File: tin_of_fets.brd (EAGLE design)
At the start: 28.6 x 55.9 mm, 49 parts, among them Q1 J112, Q2 J112, Q3 ZVN4306A, Q4 ZVN4306A, Q5 J112, Q6 J112, Q7 ZVN4306A, Q8 ZVN4306A, T1 ZTX694B

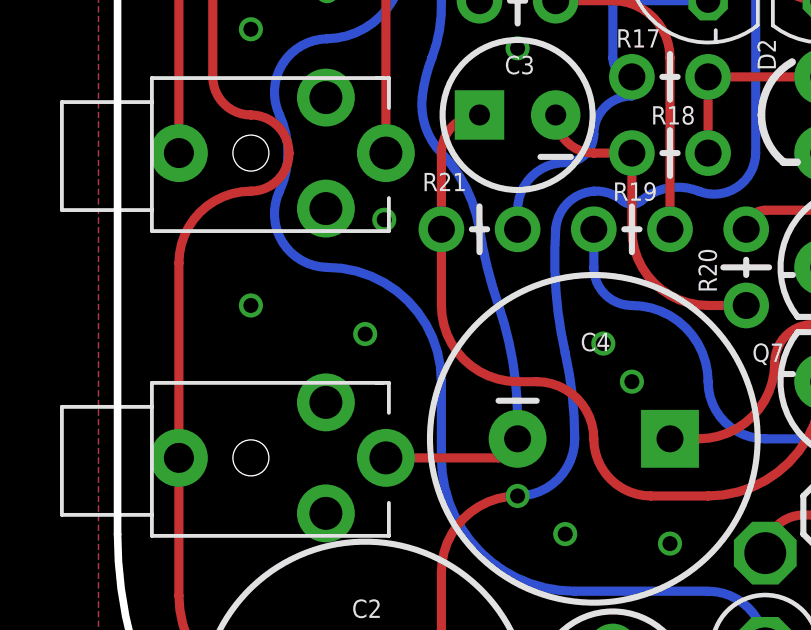
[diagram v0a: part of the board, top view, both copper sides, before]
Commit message: Single bypass cap. No more room
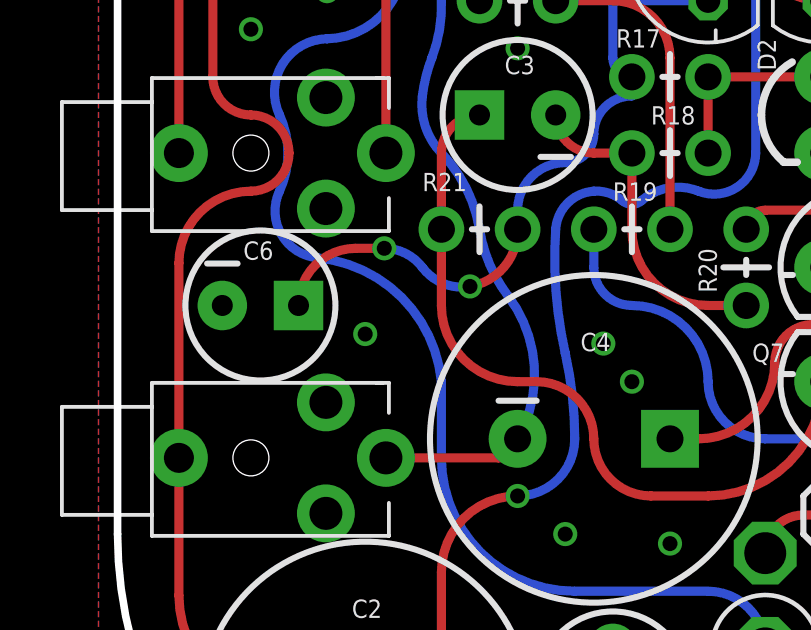
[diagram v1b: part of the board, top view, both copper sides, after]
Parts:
- added C6: 10uF, SparkFun-Capacitors:CPOL-RADIAL-10UF-25V
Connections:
- net GND: now also C6.2
- net VCC: now also C6.1
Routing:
- net VCC: track 39.2 -> 48.5 mm, vias 0 -> 2
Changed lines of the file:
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@@
 </element>
 <element name="J4" library="SparkFun-Connectors" package="STEREOJACK2.5MM_STEREOJACK2.5MM" value="" x="25.4" y="3.81" smashed="yes" rot="R90"/>
+<element name="C6" library="SparkFun-Capacitors" package="CPOL-RADIAL-10UF-25V" value="10uF" x="5.3975" y="21.59" smashed="yes">
+<attribute name="NAME" x="4.826" y="23.114" size="0.6096" layer="25" ratio="15"/>
+<attribute name="VALUE" x="3.4925" y="17.907" size="0.8128" layer="27"/>
+</element>
 </elements>
 <signals>
@@
 <via x="15.5575" y="13.97" extent="1-16" drill="0.5"/>
 <via x="8.89" y="20.6375" extent="1-16" drill="0.5"/>
-<via x="5.08" y="21.59" extent="1-16" drill="0.5"/>
-<via x="9.525" y="24.4475" extent="1-16" drill="0.5"/>
 <via x="19.05" y="7.3025" extent="1-16" drill="0.5"/>
 <via x="24.13" y="41.275" extent="1-16" drill="0.5"/>
 <via x="13.6525" y="36.83" extent="1-16" drill="0.5"/>
+<contactref element="C6" pad="2"/>
 </signal>
 <signal name="N$6">
@@
 <wire x1="17.145" y1="29.845" x2="17.78" y2="29.21" width="0.3048" layer="16" curve="90"/>
 <wire x1="20.32" y1="31.75" x2="17.145" y2="31.75" width="0.3048" layer="16"/>
+<contactref element="C6" pad="1"/>
+<wire x1="6.6675" y1="21.59" x2="8.5725" y2="23.495" width="0.3048" layer="1" curve="-90"/>
+<wire x1="8.5725" y1="23.495" x2="9.525" y2="23.495" width="0.3048" layer="1"/>
+<via x="9.525" y="23.495" extent="1-16" drill="0.5"/>
+<wire x1="10.795" y1="22.86" x2="12.3825" y2="22.225" width="0.3048" layer="16" curve="62.657368"/>
+<via x="12.3825" y="22.225" extent="1-16" drill="0.5"/>
+<wire x1="12.3825" y1="22.225" x2="13.97" y2="24.13" width="0.3048" layer="1" curve="81.33454"/>
+<wire x1="9.525" y1="23.495" x2="10.795" y2="22.86" width="0.3048" layer="16" curve="-53.130102"/>
 </signal>
 <signal name="N$5">
@@
 <wire x1="9.58" y1="16.51" x2="13.335" y2="16.51" width="0.3048" layer="1"/>
 <wire x1="13.335" y1="16.51" x2="13.97" y2="17.145" width="0.3048" layer="1" curve="90"/>
-<wire x1="13.97" y1="17.145" x2="13.97" y2="17.78" width="0.3048" layer="16"/>
-<wire x1="13.97" y1="17.78" x2="13.335" y2="21.59" width="0.3048" layer="16" curve="18.924644"/>
-<wire x1="13.335" y1="21.59" x2="12.7" y2="24.13" width="0.3048" layer="16" curve="-9.776801"/>
 <wire x1="12.7" y1="24.13" x2="11.43" y2="26.67" width="0.3048" layer="16" curve="34.834426"/>
 <wire x1="11.43" y1="26.67" x2="10.795" y2="28.575" width="0.3048" layer="16" curve="-51.094614"/>
@@
 <wire x1="12.7" y1="33.655" x2="14.9225" y2="33.9725" width="0.3048" layer="1" curve="-24.908515"/>
 <wire x1="14.9225" y1="33.9725" x2="17.4625" y2="34.925" width="0.3048" layer="1" curve="49.760343"/>
+<wire x1="12.7" y1="24.13" x2="13.6525" y2="21.9075" width="0.3048" layer="16" curve="28.101576"/>
+<wire x1="13.6525" y1="21.9075" x2="13.97" y2="17.145" width="0.3048" layer="16" curve="-66.870593"/>
 </signal>
 <signal name="+12V">
@@
 <wire x1="7.62" y1="30.48" x2="6.0325" y2="27.94" width="0.3048" layer="16" curve="114.080537"/>
 <wire x1="6.0325" y1="27.94" x2="6.0325" y2="25.4" width="0.3048" layer="16" curve="-50.069771"/>
-<wire x1="6.0325" y1="25.4" x2="7.62" y2="22.86" width="0.3048" layer="16" curve="114.080573"/>
-<wire x1="7.62" y1="22.86" x2="11.43" y2="19.05" width="0.3048" layer="16" curve="-90"/>
 <wire x1="11.43" y1="19.05" x2="11.43" y2="16.51" width="0.3048" layer="16"/>
 <wire x1="11.43" y1="16.51" x2="15.875" y2="12.065" width="0.3048" layer="16" curve="90"/>
@@
 <wire x1="22.86" y1="10.16" x2="25.0825" y2="11.43" width="0.3048" layer="1" curve="59.489763"/>
 <wire x1="25.0825" y1="11.43" x2="27.305" y2="13.335" width="0.3048" layer="1" curve="-37.776975"/>
+<wire x1="6.0325" y1="25.4" x2="7.3025" y2="23.1775" width="0.3048" layer="16" curve="109.559615"/>
+<wire x1="7.3025" y1="23.1775" x2="11.43" y2="19.05" width="0.3048" layer="16" curve="-79.049714"/>
 </signal>
 </signals>

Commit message: Added pads for hand-wiring bypass caps
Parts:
- added J3, J6: PAD-NO-THERMAL, my:PAD-NO-THERMAL
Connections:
- net GND: now also J3.P$1, J6.P$1
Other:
- board text added: "BP"
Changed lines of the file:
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@@
 <dimension x1="0.635" y1="41.91" x2="29.21" y2="55.88" x3="14.9225" y3="59.69" textsize="1.778" layer="47" dtype="horizontal"/>
 <dimension x1="14.605" y1="0" x2="13.97" y2="55.88" x3="-15.24" y3="27.94" textsize="1.778" layer="47" dtype="vertical"/>
+<wire x1="24.4475" y1="40.9575" x2="23.1775" y2="40.9575" width="0.3048" layer="21" curve="-90"/>
+<wire x1="14.605" y1="22.86" x2="10.16" y2="20.0025" width="0.3048" layer="21" curve="-99.462322"/>
+<text x="13.6525" y="20.0025" size="0.6096" layer="21" ratio="15">BP</text>
+<text x="25.0825" y="40.3225" size="0.6096" layer="21" ratio="15">BP</text>
 </plain>
 <attributes>
@@
 </element>
 <element name="R10" library="my-res" package="AXIAL-0.1-SM" value="6.8" x="22.225" y="44.45" smashed="yes" rot="R270">
-<attribute name="NAME" x="23.495" y="43.4975" size="0.6096" layer="25" font="vector" ratio="15" rot="R270"/>
+<attribute name="NAME" x="23.1775" y="44.1325" size="0.6096" layer="25" font="vector" ratio="15" rot="R270"/>
 <attribute name="VALUE" x="20.066" y="44.45" size="1.016" layer="27" font="vector" ratio="15" rot="R270"/>
 </element>
@@
 <attribute name="VALUE" x="3.4925" y="17.907" size="0.8128" layer="27"/>
 </element>
+<element name="J3" library="my" package="PAD-NO-THERMAL" value="PAD-NO-THERMAL" x="24.765" y="41.91" smashed="yes">
+<attribute name="NAME" x="25.7175" y="41.5925" size="0.6096" layer="25" ratio="15"/>
+</element>
+<element name="J6" library="my" package="PAD-NO-THERMAL" value="PAD-NO-THERMAL" x="8.89" y="20.6375"/>
 </elements>
 <signals>
@@
 <via x="19.05" y="13.6525" extent="1-16" drill="0.5"/>
 <via x="15.5575" y="13.97" extent="1-16" drill="0.5"/>
-<via x="8.89" y="20.6375" extent="1-16" drill="0.5"/>
 <via x="19.05" y="7.3025" extent="1-16" drill="0.5"/>
-<via x="24.13" y="41.275" extent="1-16" drill="0.5"/>
 <via x="13.6525" y="36.83" extent="1-16" drill="0.5"/>
 <contactref element="C6" pad="2"/>
+<contactref element="J3" pad="P$1"/>
+<contactref element="J6" pad="P$1"/>
 </signal>
 <signal name="N$6">

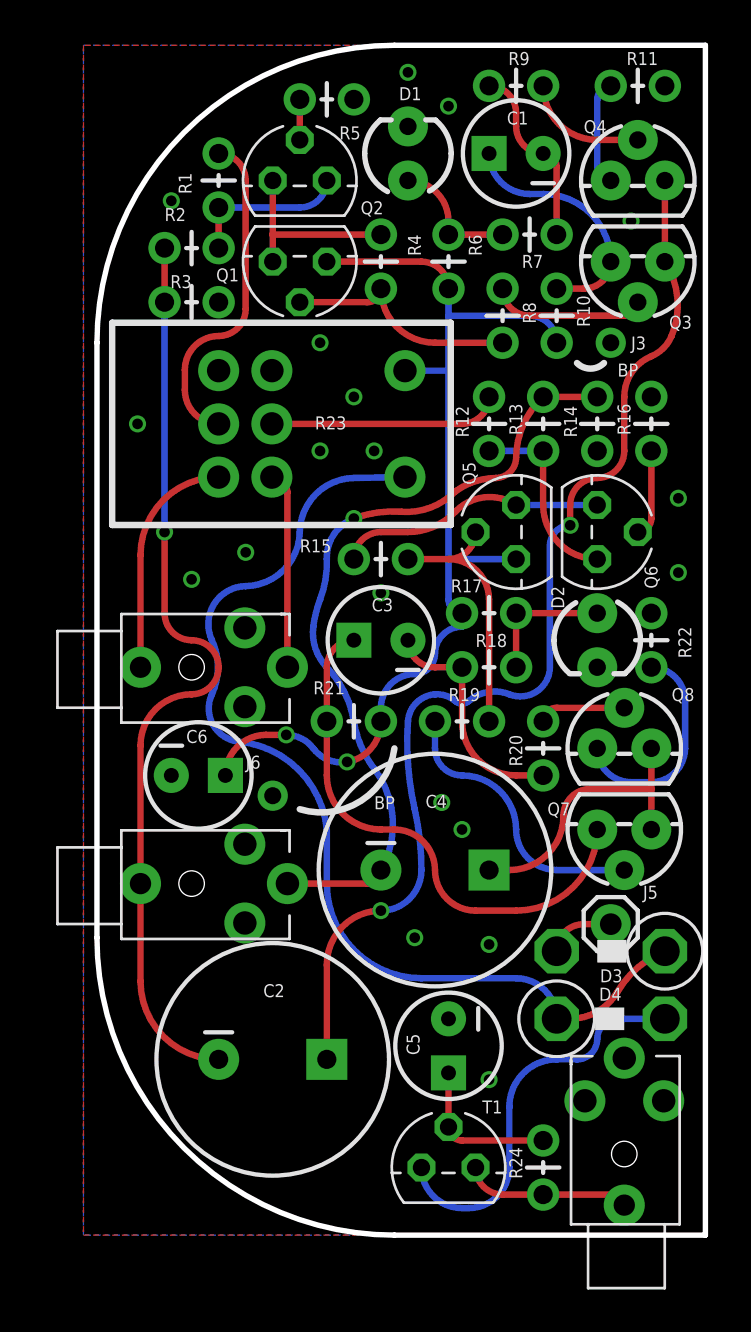
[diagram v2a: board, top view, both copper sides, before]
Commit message: Followers FB caps changed to .47u film
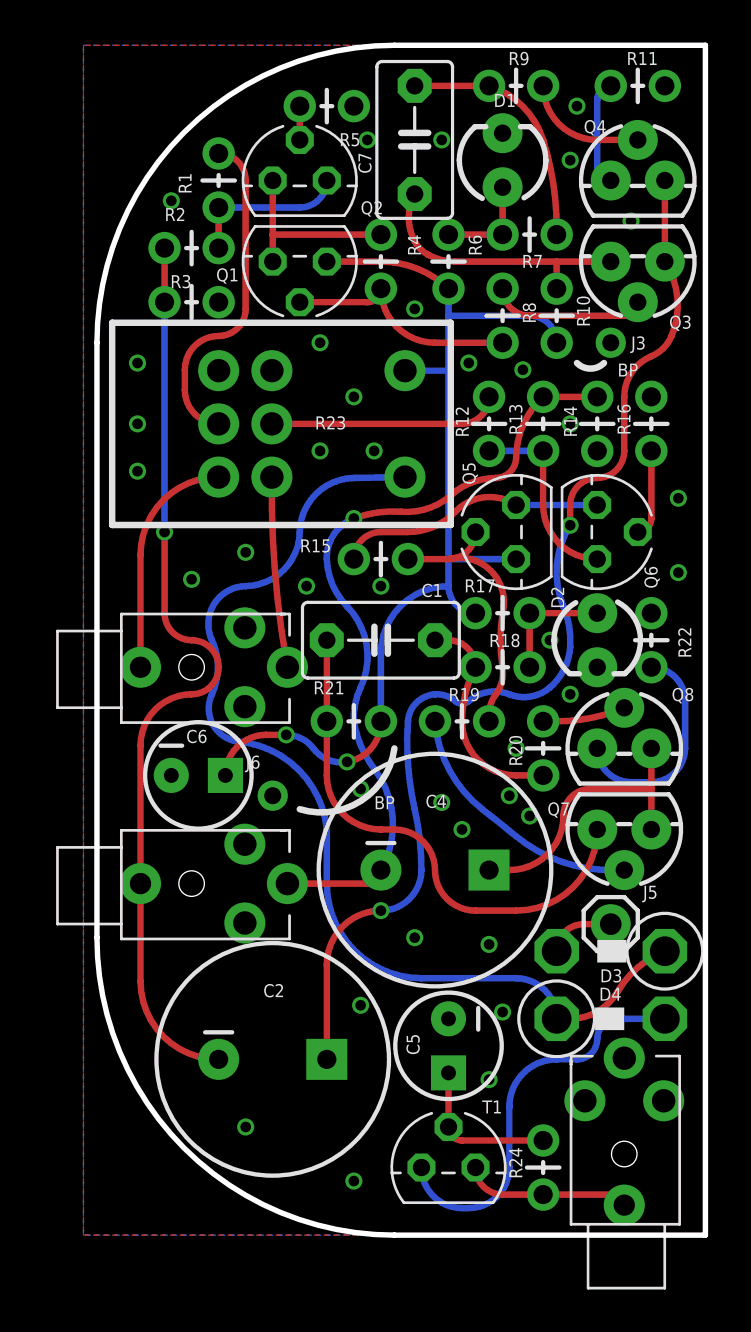
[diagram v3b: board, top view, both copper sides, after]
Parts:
- removed C3: 4.7u, SparkFun-Capacitors:CPOL-RADIAL-10UF-25V
- added C7: 0.47uF, capacitor-wima:C5B3.5
- C1: value 4.7u -> 0.47uF; device SparkFun-Capacitors:CPOL-RADIAL-10UF-25V -> capacitor-wima:C5B3.5
- R18, R7: value 100k -> 1Meg
- moved C1 23.7 mm to (14.0, 27.9), turned to 0 degrees
- moved D1 4.46 mm to (19.7, 50.5)
- moved R17 0.63 mm to (21.0, 29.2)
- moved R18 0.63 mm to (18.4, 26.7)
- moved R5 0.32 mm to (12.7, 53.0)
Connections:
- net N$11: now also C7.1; no longer C1.1
- net N$13: now also C7.2; no longer C1.2
- net N$20: now also C1.1; no longer C3.1
- net N$21: now also C1.2; no longer C3.2
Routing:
- net N$13: track 8.30 -> 11.6 mm
- net N$11: track 10.9 -> 13.0 mm
- net N$14: track 5.87 -> 4.76 mm
- net VCC: track 48.5 -> 49.5 mm
- net N$22: track 6.35 -> 5.71 mm
- net N$21: track 10.5 -> 9.91 mm
- net N$20: track 23.8 -> 23.3 mm

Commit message: Jacks pinout fixed
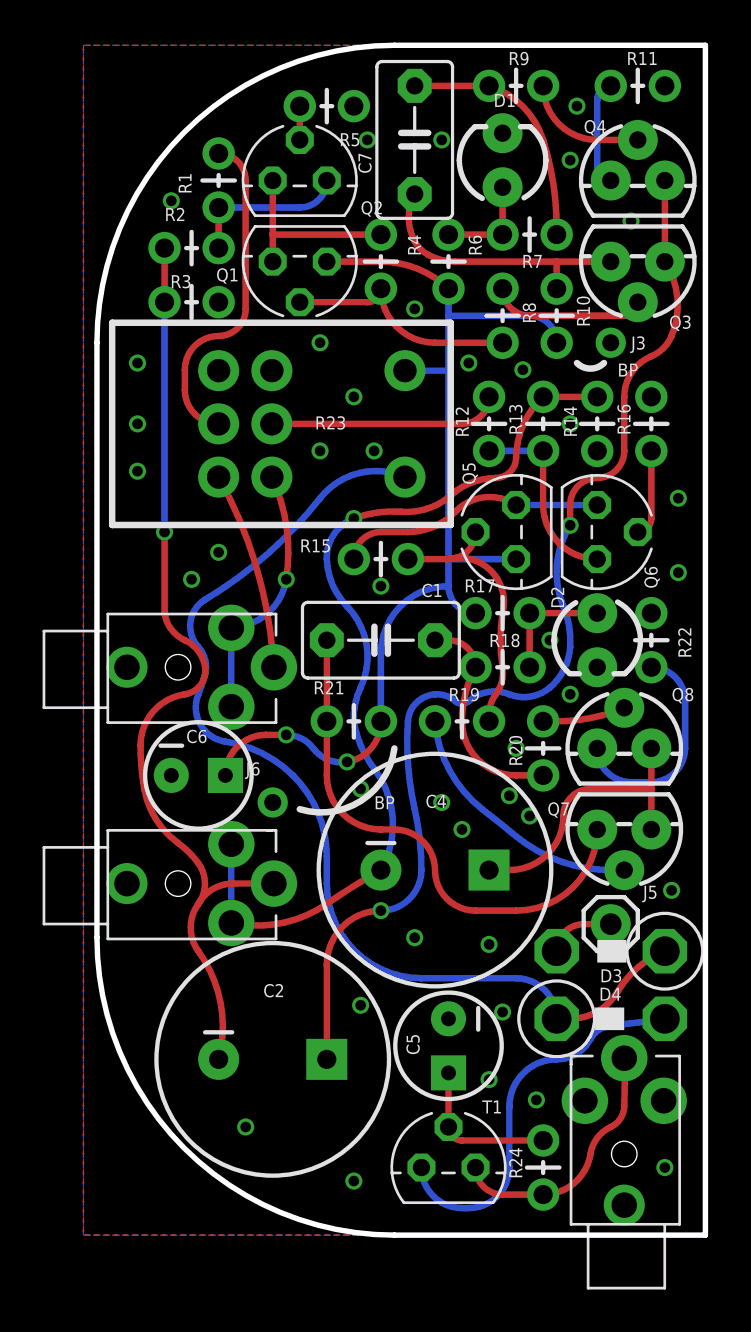
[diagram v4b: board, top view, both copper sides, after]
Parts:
- J1, J2, J4: device SparkFun-Connectors:STEREOJACK2.5MM_STEREOJACK2.5MM -> my-conn:STEREOJACK2.5MM_STEREOJACK2.5MM
- moved J1 0.63 mm to (4.45, 26.7)
- moved J2 0.63 mm to (4.45, 16.5)
- moved J6 0.32 mm to (8.89, 20.3)
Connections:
- net +12V: now also J4.TIP; no longer J4.SHIELD
- net GND: now also J1.SHIELD, J2.SHIELD, J4.RING2, J4.SHIELD; no longer J1.RING1, J2.RING1, J4.TIP
- net IN_L*: now also J1.TIP; no longer J1.SHIELD
- net IN_R*: now also J1.RING1, J1.RING2; no longer J1.TIP
- net OUT_L: now also J2.TIP; no longer J2.SHIELD
- net OUT_R: now also J2.RING1, J2.RING2; no longer J2.TIP
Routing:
- net OUT_R: track 36.0 -> 42.7 mm
- net +12V: track 7.72 -> 11.6 mm
- net IN_R*: track 8.96 -> 12.1 mm, vias 0 -> 1
- net OUT_L: track 42.2 -> 44.6 mm
- net VCC*: track 45.6 -> 46.9 mm
- net IN_L*: track 10.5 -> 9.31 mm

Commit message: Jacks pinout fixed again
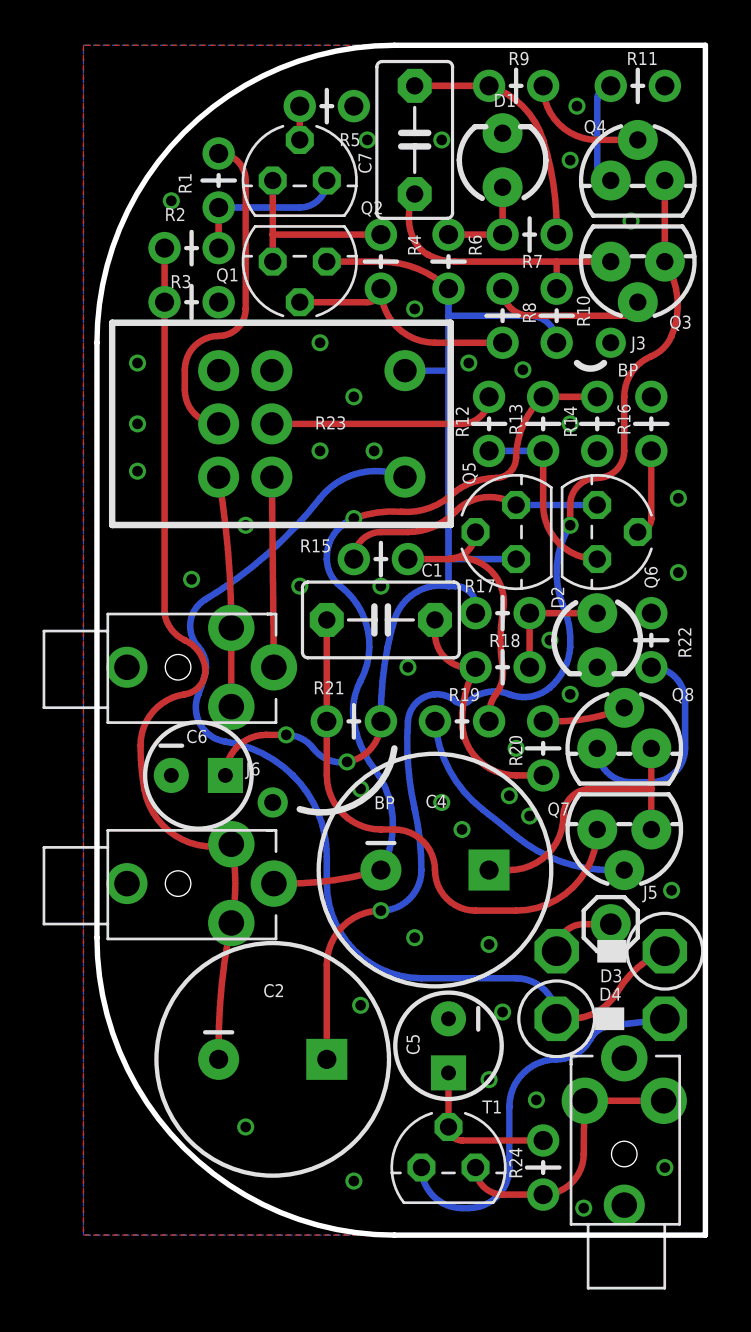
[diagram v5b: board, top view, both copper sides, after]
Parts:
- moved C1 0.95 mm to (14.0, 28.9)
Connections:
- net +12V: now also J4.TIP1, J4.TIP2; no longer J4.TIP
- net GND: now also J4.RING; no longer J4.RING1, J4.RING2
- net IN_L*: now also J1.TIP1, J1.TIP2; no longer J1.TIP
- net IN_R*: now also J1.RING; no longer J1.RING1, J1.RING2
- net OUT_L: now also J2.TIP1, J2.TIP2; no longer J2.TIP
- net OUT_R: now also J2.RING; no longer J2.RING1, J2.RING2
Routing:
- net OUT_R: track 42.7 -> 36.4 mm
- net IN_R*: track 12.1 -> 8.93 mm, vias 1 -> 0
- net OUT_L: track 44.6 -> 42.1 mm, vias 1 -> 0
- net IN_L*: track 9.31 -> 10.8 mm
- net +12V: track 11.6 -> 12.6 mm
- net N$20: track 23.3 -> 24.2 mm
- net N$21: track 9.91 -> 10.6 mm

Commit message: Small fix
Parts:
- moved C1 0.95 mm to (14.0, 27.9)
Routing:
- net N$20: track 24.2 -> 23.3 mm
- net N$21: track 10.6 -> 9.91 mm
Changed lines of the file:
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@@
 <attribute name="VALUE" x="18.8595" y="48.895" size="1.27" layer="27" ratio="10" rot="R90"/>
 </element>
-<element name="C1" library="capacitor-wima" package="C5B3.5" value="0.47uF" x="13.97" y="28.8925" smashed="yes">
-<attribute name="NAME" x="15.875" y="30.9245" size="0.6096" layer="25" ratio="15"/>
-<attribute name="VALUE" x="11.43" y="25.5905" size="1.27" layer="27" ratio="10"/>
+<element name="C1" library="capacitor-wima" package="C5B3.5" value="0.47uF" x="13.97" y="27.94" smashed="yes">
+<attribute name="NAME" x="15.875" y="29.972" size="0.6096" layer="25" ratio="15"/>
+<attribute name="VALUE" x="11.43" y="24.638" size="1.27" layer="27" ratio="10"/>
 </element>
 </elements>
@@
 <wire x1="20.32" y1="15.24" x2="24.13" y2="19.05" width="0.3048" layer="1" curve="90"/>
 <contactref element="C1" pad="1"/>
-<wire x1="11.43" y1="24.13" x2="11.43" y2="28.8925" width="0.3048" layer="1"/>
+<wire x1="11.43" y1="24.13" x2="11.43" y2="27.94" width="0.3048" layer="1"/>
 </signal>
 <signal name="N$21">
@@
 <contactref element="C1" pad="2"/>
 <wire x1="17.78" y1="24.13" x2="18.415" y2="26.67" width="0.3048" layer="1" curve="-28.072487"/>
-<wire x1="16.51" y1="28.8925" x2="16.51" y2="28.2575" width="0.3048" layer="1"/>
-<wire x1="16.51" y1="28.2575" x2="18.415" y2="26.67" width="0.3048" layer="1" curve="100.388821"/>
+<wire x1="18.415" y1="26.67" x2="17.78" y2="26.67" width="0.3048" layer="1"/>
+<wire x1="17.78" y1="26.67" x2="16.51" y2="27.94" width="0.3048" layer="1" curve="-90"/>
 </signal>
 <signal name="N$22">
